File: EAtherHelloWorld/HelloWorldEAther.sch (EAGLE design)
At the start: 3 parts

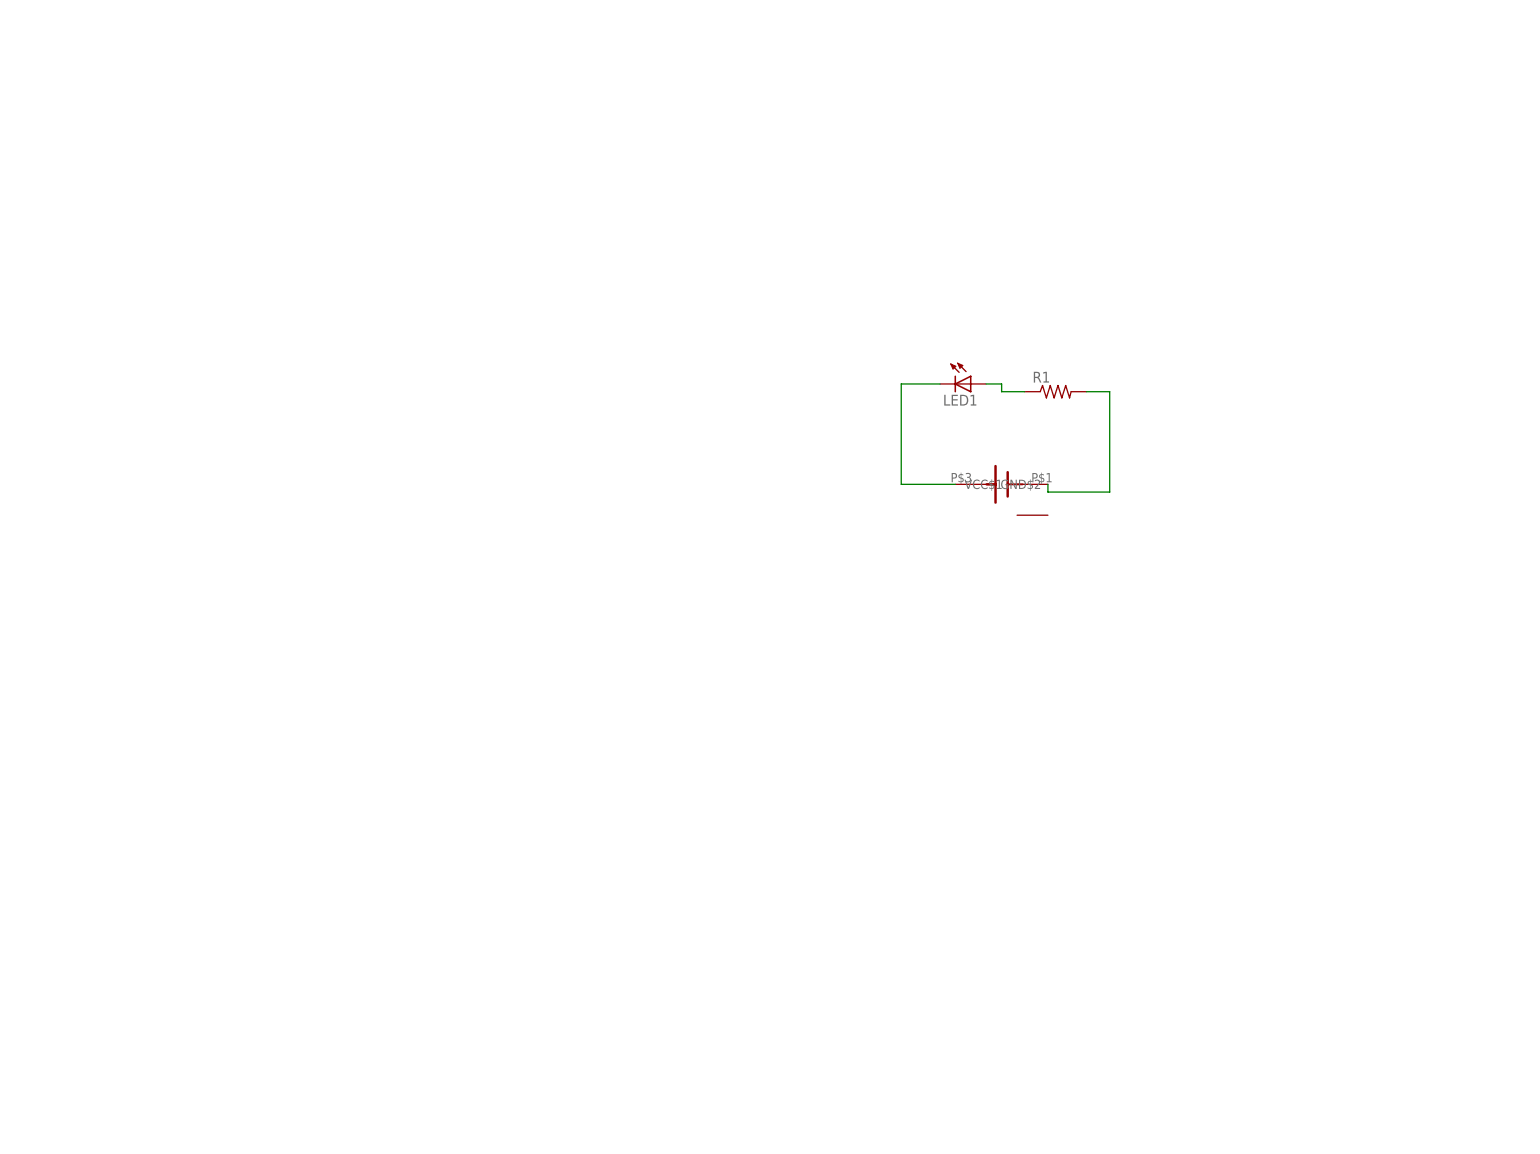
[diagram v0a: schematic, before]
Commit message: Added EA tutorial board
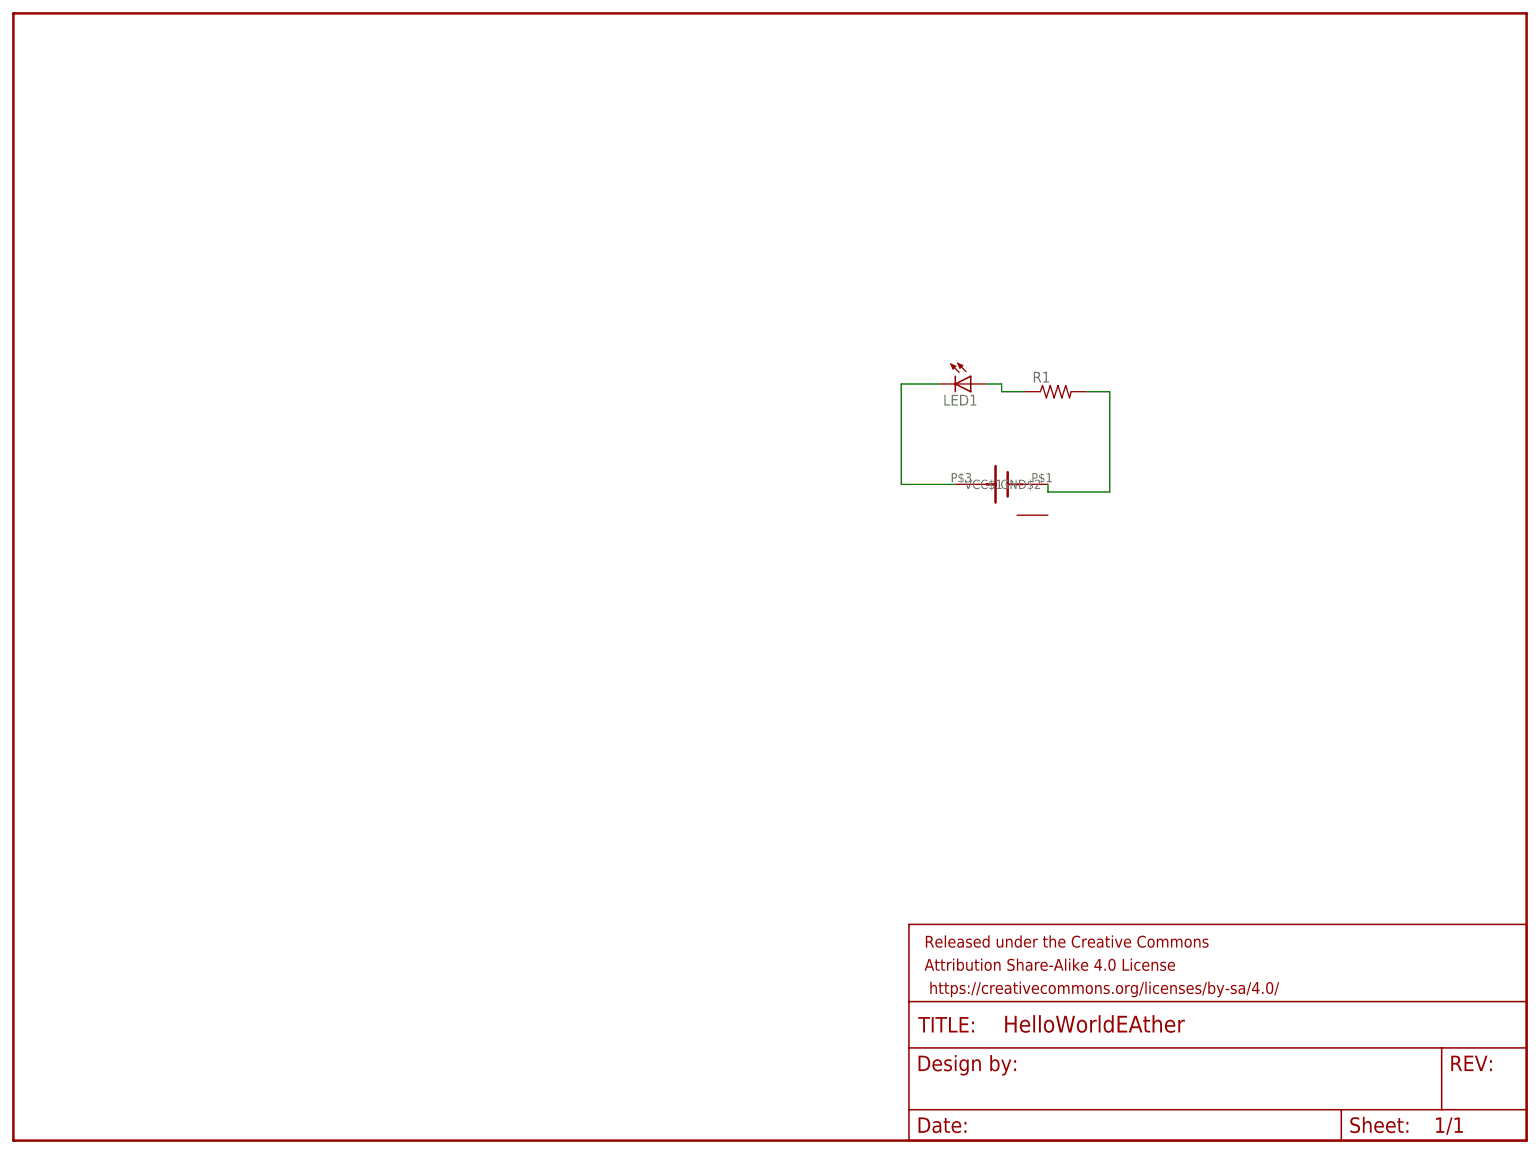
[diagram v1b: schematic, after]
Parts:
- added FRAME1: FRAME-LETTER, SparkFun-Aesthetics:FRAME-LETTER
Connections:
- net N$1 renamed BAT
- net N$2 renamed R
- net N$4 renamed LED
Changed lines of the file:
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@@
 <?xml version="1.0" encoding="utf-8"?>
 <!DOCTYPE eagle SYSTEM "eagle.dtd">
-<eagle version="6.5.0">
+<eagle version="7.7.0">
 <drawing>
 <settings>
@@
 <layers>
 <layer number="1" name="Top" color="4" fill="1" visible="no" active="no"/>
+<layer number="2" name="Route2" color="1" fill="3" visible="no" active="no"/>
+<layer number="3" name="Route3" color="4" fill="3" visible="no" active="no"/>
+<layer number="4" name="Route4" color="1" fill="4" visible="no" active="no"/>
+<layer number="5" name="Route5" color="4" fill="4" visible="no" active="no"/>
+<layer number="6" name="Route6" color="1" fill="8" visible="no" active="no"/>
+<layer number="7" name="Route7" color="4" fill="8" visible="no" active="no"/>
+<layer number="8" name="Route8" color="1" fill="2" visible="no" active="no"/>
+<layer number="9" name="Route9" color="4" fill="2" visible="no" active="no"/>
+<layer number="10" name="Route10" color="1" fill="7" visible="no" active="no"/>
+<layer number="11" name="Route11" color="4" fill="7" visible="no" active="no"/>
+<layer number="12" name="Route12" color="1" fill="5" visible="no" active="no"/>
+<layer number="13" name="Route13" color="4" fill="5" visible="no" active="no"/>
+<layer number="14" name="Route14" color="1" fill="6" visible="no" active="no"/>
+<layer number="15" name="Route15" color="4" fill="6" visible="no" active="no"/>
 <layer number="16" name="Bottom" color="1" fill="1" visible="no" active="no"/>
 <layer number="17" name="Pads" color="2" fill="1" visible="no" active="no"/>
@@
 <layer number="56" name="wert" color="7" fill="1" visible="no" active="no"/>
 <layer number="57" name="tCAD" color="7" fill="1" visible="no" active="no"/>
+<layer number="59" name="tCarbon" color="7" fill="1" visible="no" active="no"/>
+<layer number="60" name="bCarbon" color="7" fill="1" visible="no" active="no"/>
+<layer number="90" name="Modules" color="5" fill="1" visible="no" active="yes"/>
 <layer number="91" name="Nets" color="2" fill="1" visible="yes" active="yes"/>
 <layer number="92" name="Busses" color="1" fill="1" visible="yes" active="yes"/>
@@
 <layer number="111" name="LPC17xx" color="7" fill="1" visible="yes" active="yes"/>
 <layer number="112" name="tSilk" color="7" fill="1" visible="yes" active="yes"/>
+<layer number="113" name="IDFDebug" color="7" fill="1" visible="yes" active="yes"/>
 <layer number="116" name="Patch_BOT" color="9" fill="4" visible="yes" active="yes"/>
+<layer number="118" name="Rect_Pads" color="7" fill="1" visible="yes" active="yes"/>
 <layer number="121" name="_tsilk" color="7" fill="1" visible="yes" active="yes"/>
 <layer number="122" name="_bsilk" color="7" fill="1" visible="yes" active="yes"/>
@@
 <layer number="127" name="_tValues" color="7" fill="1" visible="yes" active="yes"/>
 <layer number="128" name="_bValues" color="7" fill="1" visible="yes" active="yes"/>
+<layer number="129" name="Mask" color="7" fill="1" visible="yes" active="yes"/>
 <layer number="131" name="tAdjust" color="7" fill="1" visible="no" active="yes"/>
 <layer number="132" name="bAdjust" color="7" fill="1" visible="no" active="yes"/>
@@
 <layer number="223" name="223bmp" color="24" fill="1" visible="no" active="no"/>
 <layer number="224" name="224bmp" color="25" fill="1" visible="no" active="no"/>
+<layer number="225" name="225bmp" color="7" fill="1" visible="yes" active="yes"/>
+<layer number="226" name="226bmp" color="7" fill="1" visible="yes" active="yes"/>
+<layer number="227" name="227bmp" color="7" fill="1" visible="yes" active="yes"/>
+<layer number="228" name="228bmp" color="7" fill="1" visible="yes" active="yes"/>
+<layer number="229" name="229bmp" color="7" fill="1" visible="yes" active="yes"/>
+<layer number="230" name="230bmp" color="7" fill="1" visible="yes" active="yes"/>
+<layer number="231" name="231bmp" color="7" fill="1" visible="yes" active="yes"/>
 <layer number="248" name="Housing" color="7" fill="1" visible="yes" active="yes"/>
 <layer number="249" name="Edge" color="7" fill="1" visible="yes" active="yes"/>
@@
 <layer number="251" name="SMDround" color="7" fill="1" visible="no" active="no"/>
 <layer number="254" name="cooling" color="7" fill="1" visible="yes" active="yes"/>
+<layer number="255" name="routoute" color="7" fill="1" visible="yes" active="yes"/>
 </layers>
 <schematic xreflabel="%F%N/%S.%C%R" xrefpart="/%S.%C%R">
@@
 <part name="U$1" library="battery" deviceset="CR1025" device=""/>
 <part name="LED1" library="eagle-ltspice" deviceset="LED_E" device=""/>
+<part name="FRAME1" library="SparkFun-Aesthetics" deviceset="FRAME-LETTER" device=""/>
 </parts>
 <sheets>
@@
 <instance part="U$1" gate="G$1" x="45.72" y="31.75" rot="R180"/>
 <instance part="LED1" gate="G$1" x="40.64" y="48.26" rot="R270"/>
+<instance part="FRAME1" gate="G$1" x="-116.84" y="-76.2"/>
+<instance part="FRAME1" gate="V" x="30.48" y="-76.2"/>
 </instances>
 <busses>
 </busses>
 <nets>
-<net name="N$2" class="0">
+<net name="R" class="0">
 <segment>
 <pinref part="R1" gate="G$1" pin="1"/>
@@
 </segment>
 </net>
-<net name="N$1" class="0">
+<net name="BAT" class="0">
 <segment>
 <pinref part="R1" gate="G$1" pin="2"/>
@@
 </segment>
 </net>
-<net name="N$4" class="0">
+<net name="LED" class="0">
 <segment>
 <pinref part="U$1" gate="G$1" pin="GND$2"/>
